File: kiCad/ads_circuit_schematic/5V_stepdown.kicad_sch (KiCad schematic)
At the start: 1 part, among them U5 L7805

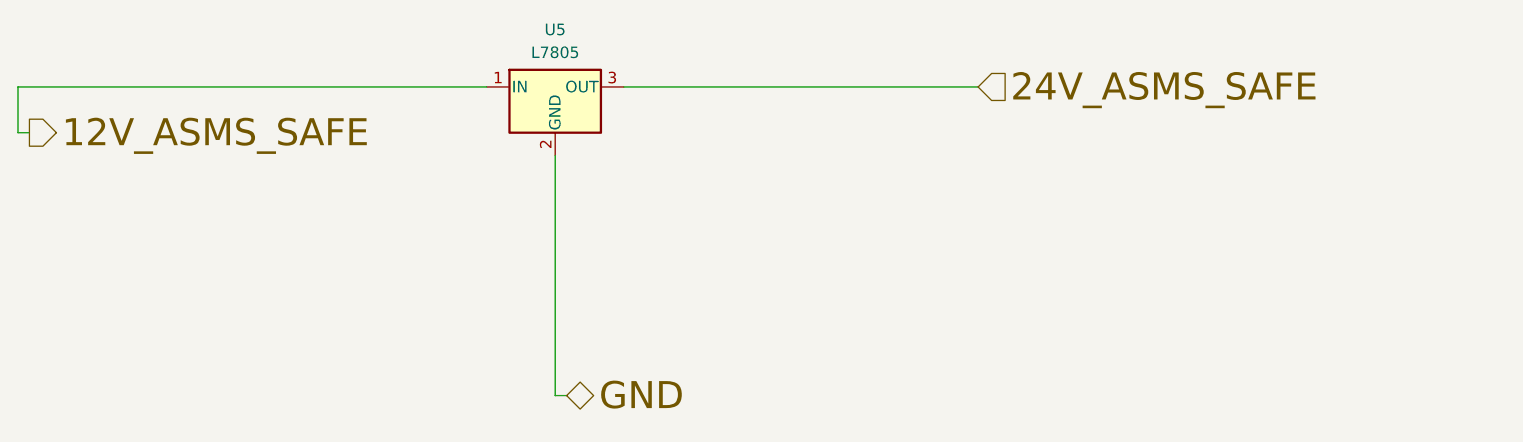
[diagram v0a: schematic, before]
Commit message: Added new symbols for linear actuators, added fuses, added 5V step down
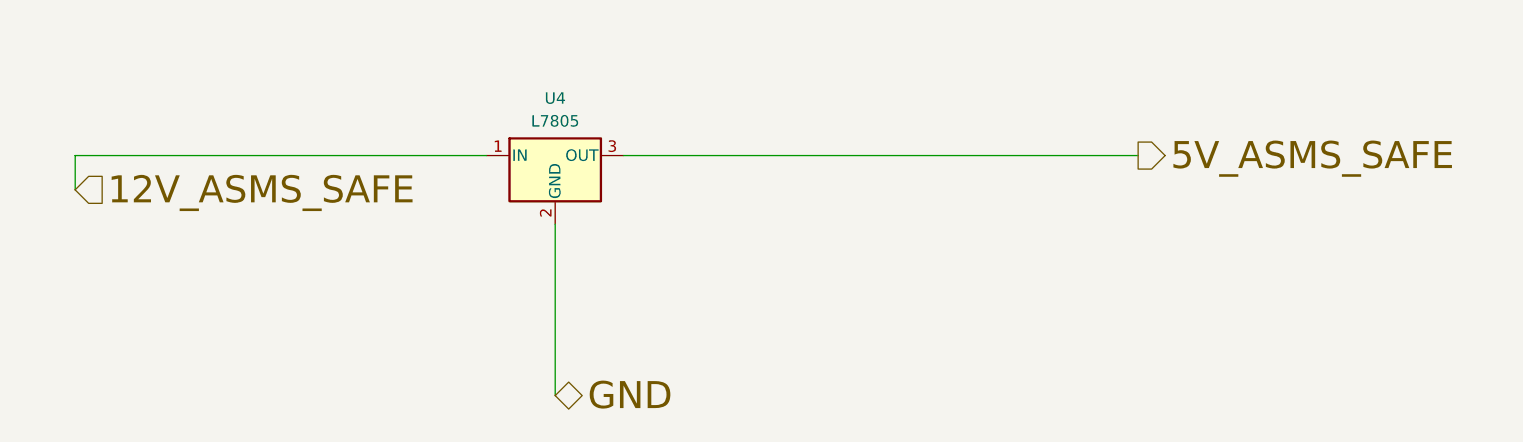
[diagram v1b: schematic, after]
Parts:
- removed U5: L7805, symbol Regulator_Linear:L7805
- added U4: L7805, symbol Regulator_Linear:L7805
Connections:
- net 12V_ASMS_SAFE: now also U4.1 (IN)
- net GND: now also U4.2 (GND)
- new net 5V_ASMS_SAFE: U4.3 (OUT)
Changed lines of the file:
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@@
 	(wire
 		(pts
-			(xy 93.98 60.96) (xy 133.35 60.96)
+			(xy 33.02 68.58) (xy 78.74 68.58)
 		)
 		(stroke
@@
 	(wire
 		(pts
-			(xy 26.67 66.04) (xy 26.67 60.96)
+			(xy 33.02 72.39) (xy 33.02 68.58)
 		)
 		(stroke
@@
 	(wire
 		(pts
-			(xy 86.36 95.25) (xy 87.63 95.25)
+			(xy 93.98 68.58) (xy 151.13 68.58)
 		)
 		(stroke
@@
 	(wire
 		(pts
-			(xy 86.36 68.58) (xy 86.36 95.25)
+			(xy 86.36 76.2) (xy 86.36 95.25)
 		)
 		(stroke
@@
 		)
 	)
-	(wire
-		(pts
-			(xy 27.94 66.04) (xy 26.67 66.04)
-		)
-		(stroke
-			(width 0)
-			(type default)
+	(hierarchical_label "GND"
+		(shape bidirectional)
+		(at 86.36 95.25 0)
+		(effects
+			(font
+				(size 3 3)
+				(color 0 0 0 1)
+			)
+			(justify left)
 		)
 	)
-	(wire
-		(pts
-			(xy 26.67 60.96) (xy 78.74 60.96)
-		)
-		(stroke
-			(width 0)
-			(type default)
+	(hierarchical_label "5V_ASMS_SAFE"
+		(shape output)
+		(at 151.13 68.58 0)
+		(effects
+			(font
+				(size 3 3)
+				(color 255 0 0 1)
+			)
+			(justify left)
 		)
 	)
 	(hierarchical_label "12V_ASMS_SAFE"
-		(shape output)
-		(at 27.94 66.04 0)
+		(shape input)
+		(at 33.02 72.39 0)
 		(effects
 			(font
@@
 		)
 	)
-	(hierarchical_label "GND"
-		(shape bidirectional)
-		(at 87.63 95.25 0)
-		(effects
-			(font
-				(size 3 3)
-				(color 0 0 0 1)
-			)
-			(justify left)
-		)
-	)
-	(hierarchical_label "24V_ASMS_SAFE"
-		(shape input)
-		(at 133.35 60.96 0)
-		(effects
-			(font
-				(size 3 3)
-				(color 255 0 0 1)
-			)
-			(justify left)
-		)
-	)
 	(symbol
 		(lib_id "Regulator_Linear:L7805")
-		(at 86.36 60.96 0)
+		(at 86.36 68.58 0)
 		(unit 1)
 		(exclude_from_sim no)
@@
 		(dnp no)
 		(fields_autoplaced yes)
-		(property "Reference" "U5"
-			(at 86.36 54.61 0)
+		(property "Reference" "U4"
+			(at 86.36 62.23 0)
 			(effects
 				(font
@@
 		)
 		(property "Value" "L7805"
-			(at 86.36 57.15 0)
+			(at 86.36 64.77 0)
 			(effects
 				(font
@@
 		)
 		(property "Footprint" ""
-			(at 86.995 64.77 0)
+			(at 86.995 72.39 0)
 			(effects
 				(font
@@
 		)
 		(property "Datasheet" "http://www.st.com/content/ccc/resource/technical/document/datasheet/41/4f/b3/b0/12/d4/47/88/CD00000444.pdf/files/CD00000444.pdf/jcr:content/translations/en.CD00000444.pdf"
-			(at 86.36 62.23 0)
+			(at 86.36 69.85 0)
 			(effects
 				(font
@@
 		)
 		(property "Description" "Positive 1.5A 35V Linear Regulator, Fixed Output 5V, TO-220/TO-263/TO-252"
-			(at 86.36 60.96 0)
+			(at 86.36 68.58 0)
 			(effects
 				(font
@@
 		)
 		(instances
-			(project "ads_circuit_schematic"
-				(path "/71fa6abf-14fe-4383-b55d-b9c0203d051b/6b6cd35a-2bfb-49a2-8edb-a39cb5d21f2f"
-					(reference "U5")
+			(project ""
+				(path "/71fa6abf-14fe-4383-b55d-b9c0203d051b/5e4e8b56-65cb-49b7-9084-2612933c5688"
+					(reference "U4")
 					(unit 1)
 				)
